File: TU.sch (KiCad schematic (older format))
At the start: 6 parts, among them J1 Conn_01x06_Male, J2 Conn_01x17_Male, J3 Conn_01x05_Male, J4 Debugger connector, J6 Conn_01x05_Male

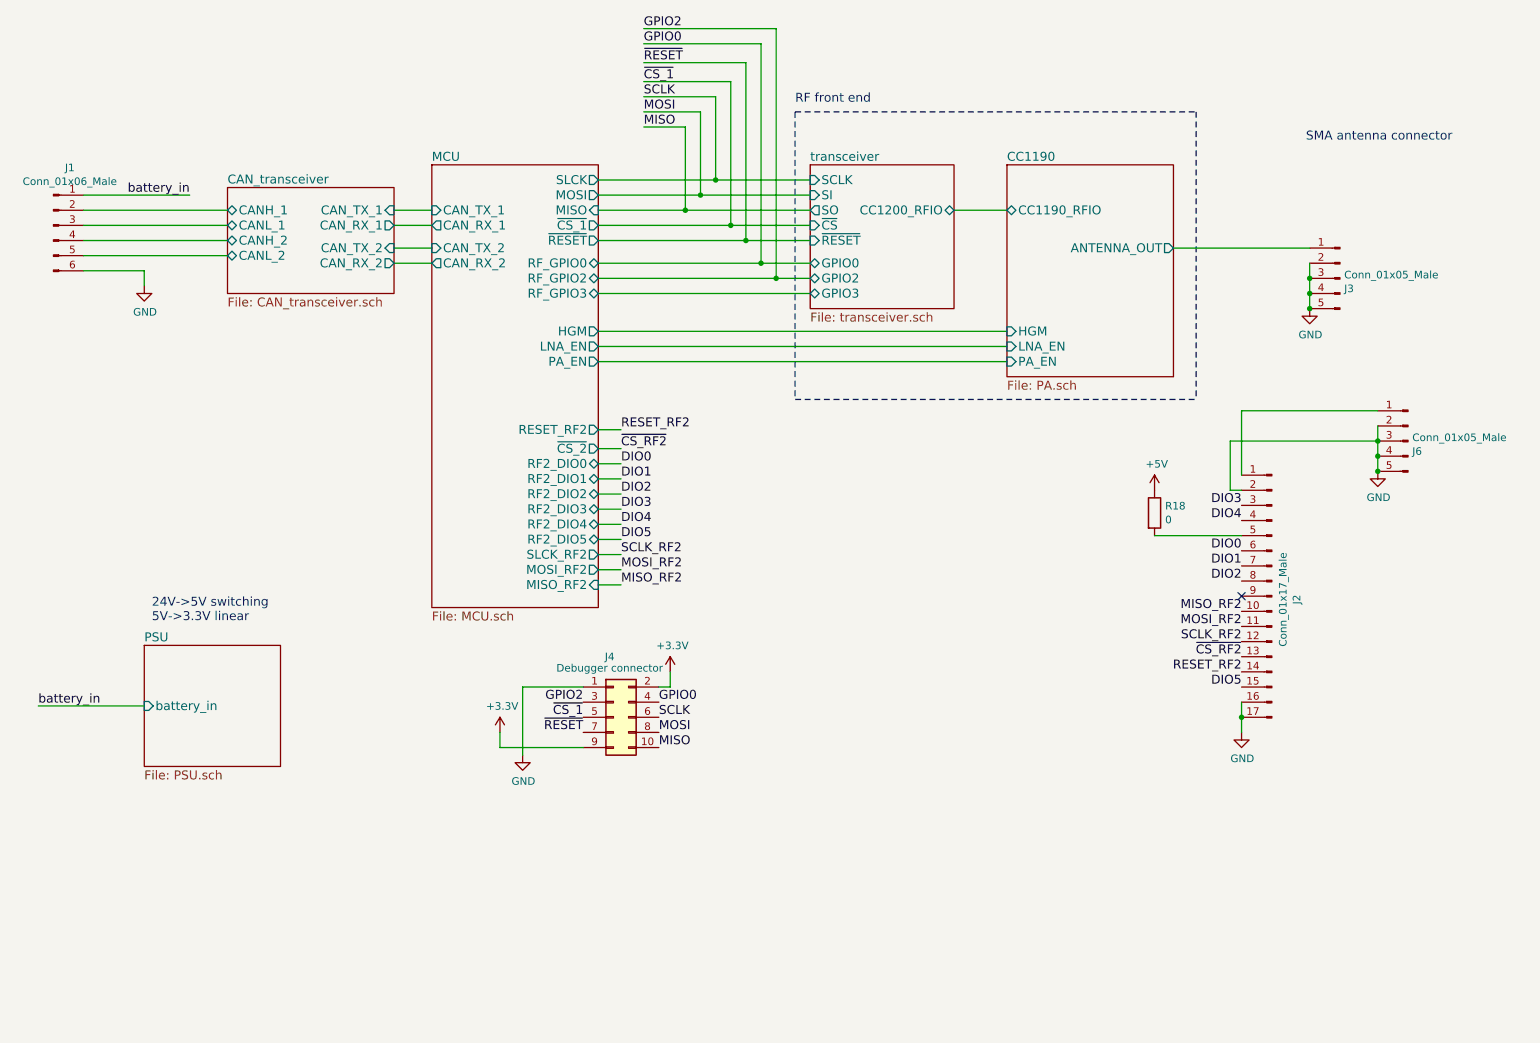
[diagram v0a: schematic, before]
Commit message: Added mounting holes and terminal block
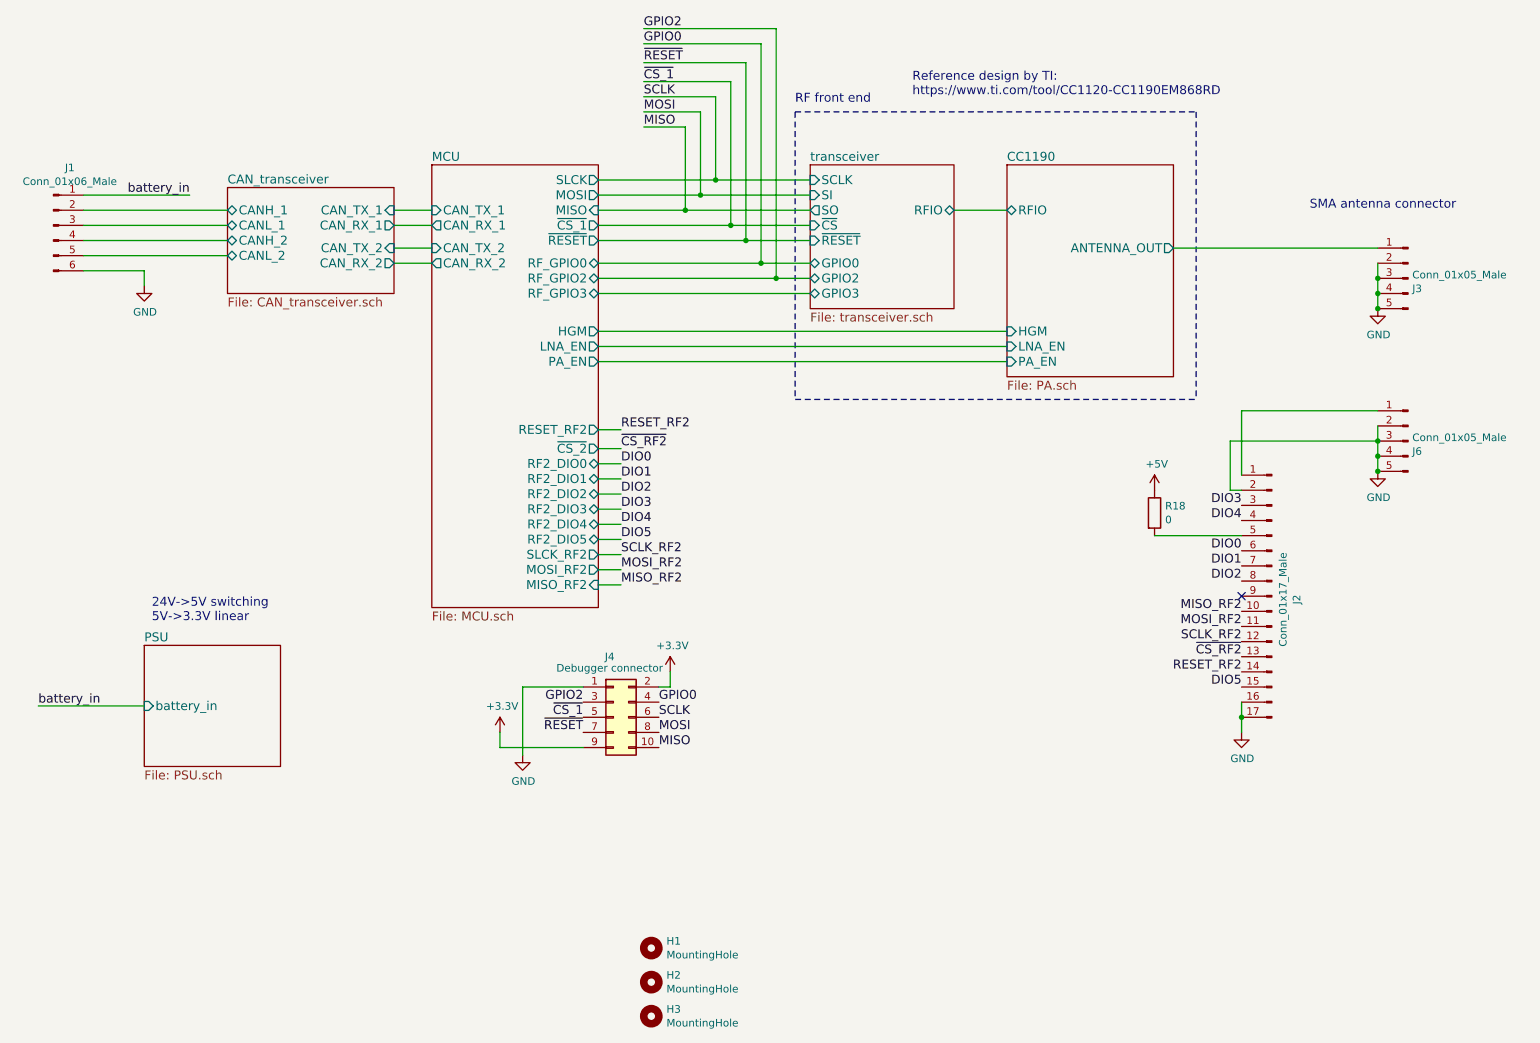
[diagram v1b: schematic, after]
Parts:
- added H1, H2, H3: MountingHole, MountingHole:MountingHole_2.5mm, symbol Mechanical:MountingHole
- J1: footprint Connector_PinHeader_2.54mm:PinHeader_1x06_P2.54mm_Vertical -> TU-HW RF LIB:TE_282834-6
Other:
- note added: "Reference design by TI:\nhttps://www.ti.com/tool/CC1120-CC1190EM868RD\n"
- moved on the sheet: J3
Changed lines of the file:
@@
 Text Notes 6100 1500 0    59   ~ 0
 RF front end\n
-Text Notes 9475 1750 0    59   ~ 0
+Text Notes 9500 2200 0    59   ~ 0
 SMA antenna connector
 $Comp
@@
 F 0 "J1" H 1308 2681 50  0000 C CNN
 F 1 "Conn_01x06_Male" H 1308 2590 50  0000 C CNN
-F 2 "Connector_PinHeader_2.54mm:PinHeader_1x06_P2.54mm_Vertical" H 1200 2300 50  0001 C CNN
+F 2 "TU-HW RF LIB:TE_282834-6" H 1200 2300 50  0001 C CNN
 F 3 "~" H 1200 2300 50  0001 C CNN
 	1    1200 2300
@@
 Wire Notes Line
 	6100 1550 6100 3450
-$Sheet
-S 7500 1900 1100 1400
-U 6014566F
-F0 "CC1190" 59
-F1 "PA.sch" 59
-F2 "HGM" I L 7500 3000 59
-F3 "LNA_EN" I L 7500 3100 59
-F4 "PA_EN" I L 7500 3200 59
-F5 "ANTENNA_OUT" O R 8600 2450 59
-F6 "CC1190_RFIO" B L 7500 2200 59
-$EndSheet
 Wire Wire Line
 	3450 2200 3700 2200
@@
 Wire Wire Line
 	7150 2200 7500 2200
-Wire Wire Line
-	8600 2450 9500 2450
 $Sheet
 S 6200 1900 950  950
@@
 F8 "GPIO2" B L 6200 2650 59
 F9 "GPIO3" B L 6200 2750 59
-F10 "CC1200_RFIO" B R 7150 2200 59
+F10 "RFIO" B R 7150 2200 59
 $EndSheet
 $Comp
@@
 L Connector:Conn_01x05_Male J3
 U 1 1 6040F77B
-P 9700 2650
-F 0 "J3" H 9672 2582 50  0000 R CNN
-F 1 "Conn_01x05_Male" H 9672 2673 50  0000 R CNN
-F 2 "TU-HW RF LIB:Wurth_SMA_60312002114503" H 9700 2650 50  0001 C CNN
-F 3 "~" H 9700 2650 50  0001 C CNN
-	1    9700 2650
+P 10150 2650
+F 0 "J3" H 10122 2582 50  0000 R CNN
+F 1 "Conn_01x05_Male" H 10122 2673 50  0000 R CNN
+F 2 "TU-HW RF LIB:Wurth_SMA_60312002114503" H 10150 2650 50  0001 C CNN
+F 3 "~" H 10150 2650 50  0001 C CNN
+	1    10150 2650
 	-1   0    0    -1
 $EndComp
@@
 Wire Wire Line
 	8975 3725 9950 3725
-Wire Wire Line
-	9500 2550 9500 2650
-Connection ~ 9500 2650
-Wire Wire Line
-	9500 2650 9500 2750
-Connection ~ 9500 2750
-Wire Wire Line
-	9500 2750 9500 2850
 $Comp
 L power:GND #PWR01
 U 1 1 604243F5
-P 9500 2850
-F 0 "#PWR01" H 9500 2600 50  0001 C CNN
-F 1 "GND" H 9505 2677 50  0000 C CNN
-F 2 "" H 9500 2850 50  0001 C CNN
-F 3 "" H 9500 2850 50  0001 C CNN
-	1    9500 2850
-	1    0    0    -1
-$EndComp
-Connection ~ 9500 2850
+P 9950 2850
+F 0 "#PWR01" H 9950 2600 50  0001 C CNN
+F 1 "GND" H 9955 2677 50  0000 C CNN
+F 2 "" H 9950 2850 50  0001 C CNN
+F 3 "" H 9950 2850 50  0001 C CNN
+	1    9950 2850
+	1    0    0    -1
+$EndComp
 Wire Wire Line
 	4800 2000 5575 2000
@@
 Wire Wire Line
 	5100 1000 5975 1000
+Text Notes 6875 1450 0    59   ~ 0
+Reference design by TI:\nhttps://www.ti.com/tool/CC1120-CC1190EM868RD\n
+Wire Wire Line
+	9950 2550 9950 2650
+Wire Wire Line
+	8600 2450 9950 2450
+Connection ~ 9950 2650
+Wire Wire Line
+	9950 2650 9950 2750
+Connection ~ 9950 2750
+Wire Wire Line
+	9950 2750 9950 2850
+Connection ~ 9950 2850
+$Comp
+L Mechanical:MountingHole H1
+U 1 1 602E5094
+P 5150 7075
+F 0 "H1" H 5250 7121 50  0000 L CNN
+F 1 "MountingHole" H 5250 7030 50  0000 L CNN
+F 2 "MountingHole:MountingHole_2.5mm" H 5150 7075 50  0001 C CNN
+F 3 "~" H 5150 7075 50  0001 C CNN
+	1    5150 7075
+	1    0    0    -1
+$EndComp
+$Comp
+L Mechanical:MountingHole H2
+U 1 1 602E5AB8
+P 5150 7300
+F 0 "H2" H 5250 7346 50  0000 L CNN
+F 1 "MountingHole" H 5250 7255 50  0000 L CNN
+F 2 "MountingHole:MountingHole_2.5mm" H 5150 7300 50  0001 C CNN
+F 3 "~" H 5150 7300 50  0001 C CNN
+	1    5150 7300
+	1    0    0    -1
+$EndComp
+$Comp
+L Mechanical:MountingHole H3
+U 1 1 602E7750
+P 5150 7525
+F 0 "H3" H 5250 7571 50  0000 L CNN
+F 1 "MountingHole" H 5250 7480 50  0000 L CNN
+F 2 "MountingHole:MountingHole_2.5mm" H 5150 7525 50  0001 C CNN
+F 3 "~" H 5150 7525 50  0001 C CNN
+	1    5150 7525
+	1    0    0    -1
+$EndComp
+$Sheet
+S 7500 1900 1100 1400
+U 6014566F
+F0 "CC1190" 59
+F1 "PA.sch" 59
+F2 "HGM" I L 7500 3000 59
+F3 "LNA_EN" I L 7500 3100 59
+F4 "PA_EN" I L 7500 3200 59
+F5 "ANTENNA_OUT" O R 8600 2450 59
+F6 "RFIO" B L 7500 2200 59
+$EndSheet
 $EndSCHEMATC

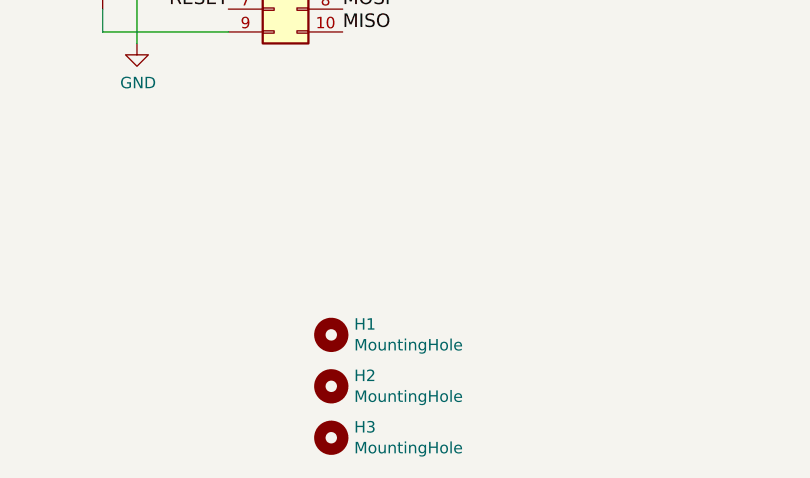
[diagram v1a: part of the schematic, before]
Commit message: Made sections clearer and cleaned up silkscreen.
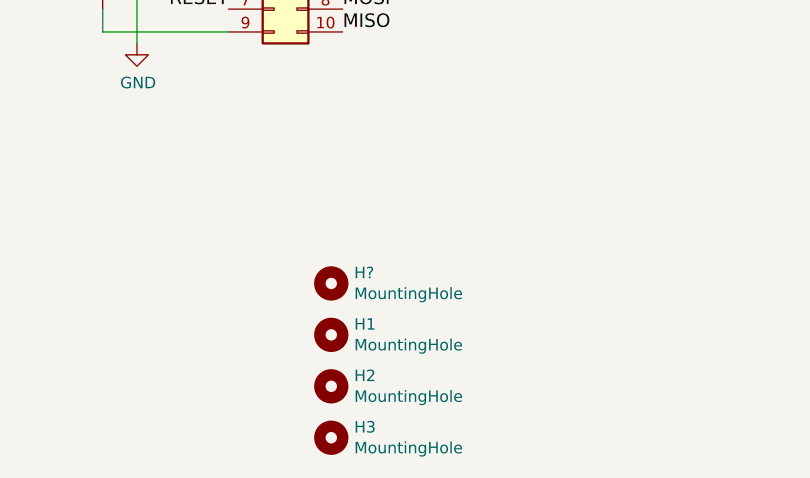
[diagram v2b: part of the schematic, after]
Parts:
- added H?: MountingHole, MountingHole:MountingHole_2.5mm, symbol Mechanical:MountingHole
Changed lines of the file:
@@
 F6 "RFIO" B L 7500 2200 59
 $EndSheet
+$Comp
+L Mechanical:MountingHole H?
+U 1 1 60308938
+P 5150 6850
+F 0 "H?" H 5250 6896 50  0000 L CNN
+F 1 "MountingHole" H 5250 6805 50  0000 L CNN
+F 2 "MountingHole:MountingHole_2.5mm" H 5150 6850 50  0001 C CNN
+F 3 "~" H 5150 6850 50  0001 C CNN
+	1    5150 6850
+	1    0    0    -1
+$EndComp
 $EndSCHEMATC

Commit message: Added PA shield
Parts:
- gave numbers to parts that had none: 1
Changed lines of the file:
@@
 $EndSheet
 $Comp
-L Mechanical:MountingHole H?
+L Mechanical:MountingHole H4
 U 1 1 60308938
 P 5150 6850
-F 0 "H?" H 5250 6896 50  0000 L CNN
+F 0 "H4" H 5250 6896 50  0000 L CNN
 F 1 "MountingHole" H 5250 6805 50  0000 L CNN
 F 2 "MountingHole:MountingHole_2.5mm" H 5150 6850 50  0001 C CNN

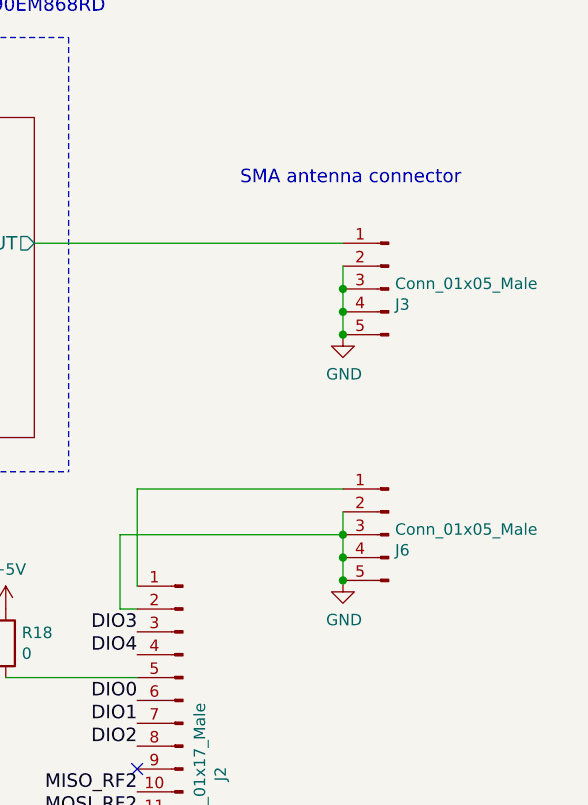
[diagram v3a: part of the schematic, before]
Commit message: Added guard ring and cleaned up silkscreen
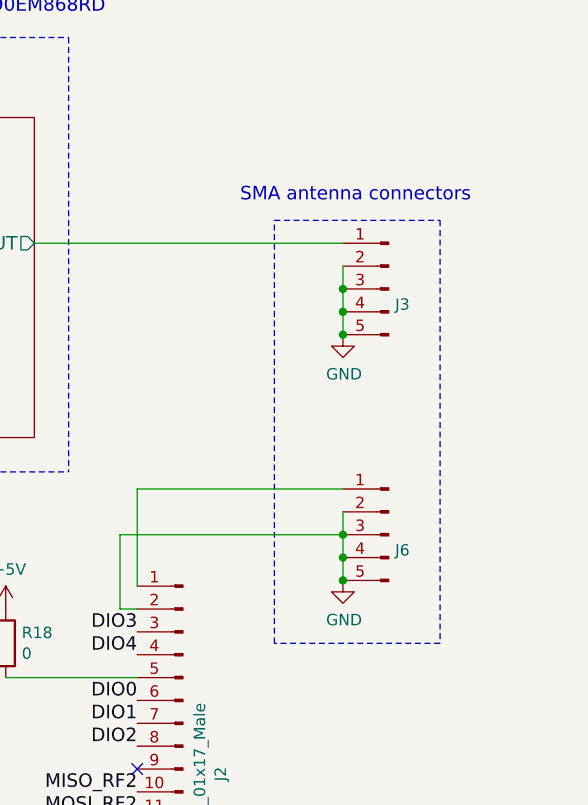
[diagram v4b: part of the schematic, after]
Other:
- note added: "SMA antenna connectors\n"
- note removed: "SMA antenna connector"
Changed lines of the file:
@@
 Text Notes 6100 1500 0    59   ~ 0
 RF front end\n
-Text Notes 9500 2200 0    59   ~ 0
-SMA antenna connector
+Text Notes 9500 2275 0    59   ~ 0
+SMA antenna connectors\n
 $Comp
 L Connector:Conn_01x06_Male J1
@@
 Wire Wire Line
 	8475 4350 9050 4350
-Text Label 4950 4175 0    59   ~ 0
-DIO3
-Text Label 4950 4275 0    59   ~ 0
-DIO4
-Text Label 4950 3875 0    59   ~ 0
-DIO0
-Text Label 4950 3975 0    59   ~ 0
-DIO1
-Text Label 4950 4075 0    59   ~ 0
-DIO2
-Text Label 4950 4375 0    59   ~ 0
-DIO5
 Wire Wire Line
 	4950 3875 4800 3875
@@
 Wire Wire Line
 	4950 4375 4800 4375
-Text Label 4950 3775 0    59   ~ 0
-~CS_RF2
 Wire Wire Line
 	4950 3775 4800 3775
-Text Label 4950 3650 0    59   ~ 0
-RESET_RF2
-Wire Wire Line
-	4950 3650 4800 3650
 Wire Wire Line
 	5775 2400 5775 1225
@@
 P 10150 2650
 F 0 "J3" H 10122 2582 50  0000 R CNN
-F 1 "Conn_01x05_Male" H 10122 2673 50  0000 R CNN
+F 1 "Conn_01x05_Male" H 10122 2673 50  0001 R CNN
 F 2 "TU-HW RF LIB:Wurth_SMA_60312002114503" H 10150 2650 50  0001 C CNN
 F 3 "~" H 10150 2650 50  0001 C CNN
@@
 P 10150 3725
 F 0 "J6" H 10122 3657 50  0000 R CNN
-F 1 "Conn_01x05_Male" H 10122 3748 50  0000 R CNN
+F 1 "Conn_01x05_Male" H 10122 3748 50  0001 R CNN
 F 2 "TU-HW RF LIB:Wurth_SMA_60312002114503" H 10150 3725 50  0001 C CNN
 F 3 "~" H 10150 3725 50  0001 C CNN
@@
 Wire Wire Line
 	4800 2200 5375 2200
-Text Label 4950 4675 0    59   ~ 0
-MISO_RF2
-Text Label 4950 4575 0    59   ~ 0
-MOSI_RF2
-Text Label 4950 4475 0    59   ~ 0
-SCLK_RF2
 Wire Wire Line
 	4800 4475 4950 4475
@@
 	1    0    0    -1
 $EndComp
+Wire Notes Line
+	10375 2350 10375 4200
+Wire Notes Line
+	10375 4200 9650 4200
+Wire Notes Line
+	9650 4200 9650 2350
+Wire Notes Line
+	9650 2350 10375 2350
+Wire Wire Line
+	4950 3650 4800 3650
+Text Label 4950 4475 0    59   ~ 0
+SCLK_RF2
+Text Label 4950 4575 0    59   ~ 0
+MOSI_RF2
+Text Label 4950 4675 0    59   ~ 0
+MISO_RF2
+Text Label 4950 3650 0    59   ~ 0
+RESET_RF2
+Text Label 4950 3775 0    59   ~ 0
+~CS_RF2
+Text Label 4950 4375 0    59   ~ 0
+DIO5
+Text Label 4950 4075 0    59   ~ 0
+DIO2
+Text Label 4950 3975 0    59   ~ 0
+DIO1
+Text Label 4950 3875 0    59   ~ 0
+DIO0
+Text Label 4950 4275 0    59   ~ 0
+DIO4
+Text Label 4950 4175 0    59   ~ 0
+DIO3
 $EndSCHEMATC
